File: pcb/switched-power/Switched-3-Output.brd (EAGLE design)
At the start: 100 x 80 mm, 39 parts, among them SW1 SPDT-100SP4, SW2 SPDT-100SP4, SW3 SPDT-100SP4

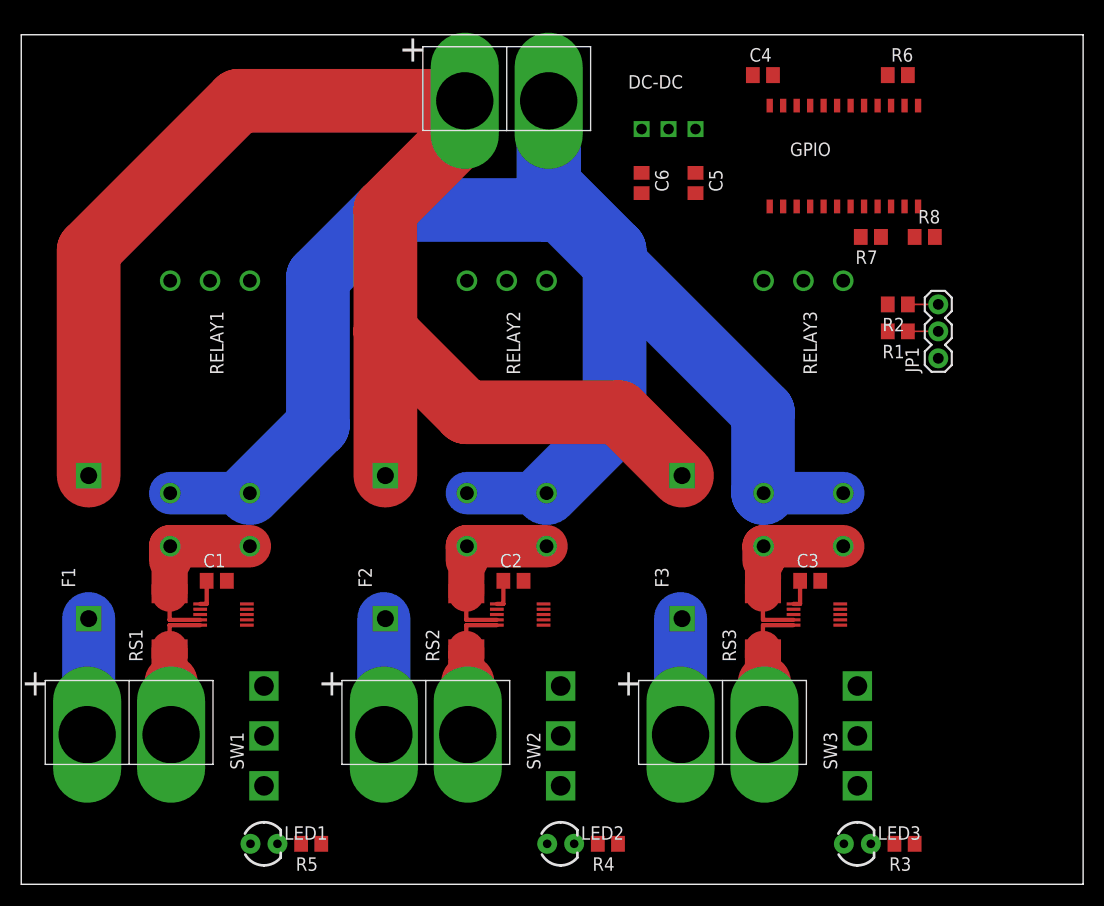
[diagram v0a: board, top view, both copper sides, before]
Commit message: Add gitignore, plus make new revision with latest board
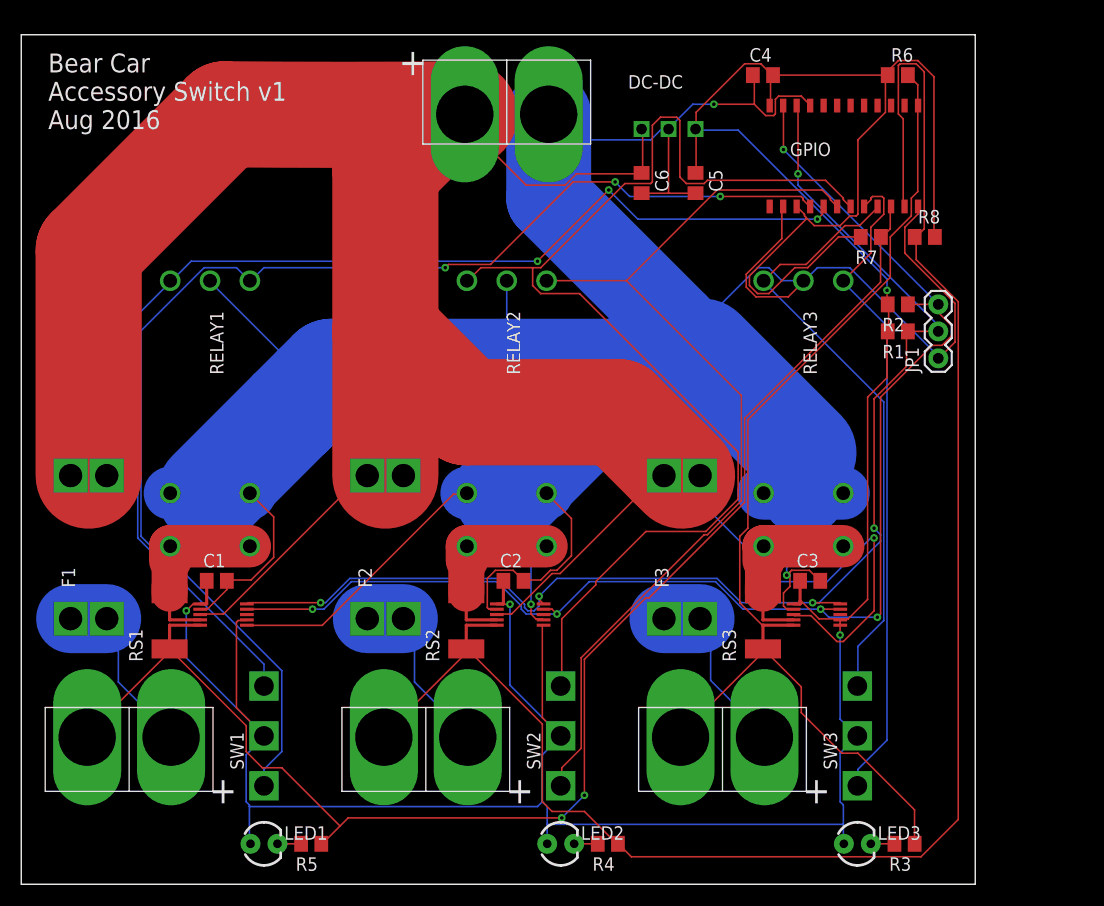
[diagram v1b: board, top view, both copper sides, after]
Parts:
- R1, R2: value (none) -> 2k
- R3, R4, R5: value (none) -> 97.6
- R6, R7, R8: value (none) -> 5k
- moved VSW1 2.54 mm to (10.2, 12.7), turned to 180 degrees
- moved VSW2 2.54 mm to (38.1, 12.7), turned to 180 degrees
- moved VSW3 2.54 mm to (66.0, 12.7), turned to 180 degrees
- moved PWR 1.27 mm to (45.7, 73.7)
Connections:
- removed net N$15: GPIO.1
- net V24: now also F1.B@1, F1.B@2, F2.B@1, F2.B@2, F3.B@1, F3.B@2; no longer F1.P$2, F2.P$2, F3.P$2
- net VSW1+: now also F1.A@1, F1.A@2; no longer F1.P$1
- net VSW2+: now also F2.A@1, F2.A@2; no longer F2.P$1
- net VSW3+: now also F3.A@1, F3.A@2; no longer F3.P$1
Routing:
- net V5: track 8.37 -> 320.8 mm, vias 0 -> 4
- net GND: track 167.5 -> 366.2 mm, vias 0 -> 3
- net VSW2-: track 14.0 -> 166.5 mm
- net SDA: track 2.86 -> 128.9 mm, vias 0 -> 5
- net VSW1-: track 14.0 -> 136.1 mm, vias 0 -> 2
- net V24: track 134.4 -> 255.2 mm, vias 0 -> 1
- net RLY1-ON: track 0.00 -> 120.3 mm, vias 0 -> 3
- net SCL: track 2.86 -> 121.9 mm, vias 0 -> 5
- net RLY2-OFF: track 0.00 -> 112.4 mm
- net RLY1-OFF: track 0.00 -> 111.4 mm, vias 0 -> 3
- net RLY2-ON: track 0.00 -> 91.0 mm
- net VSW3-: track 14.0 -> 102.6 mm
- net RLY3-ON: track 0.00 -> 62.2 mm
- net RLY3-OFF: track 0.00 -> 57.5 mm
- net VSW2+: track 11.1 -> 18.4 mm
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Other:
- board size 100 x 80 mm -> 89.8 x 80 mm
- board text added: "Bear Car Accessory Switch v1 Aug 2016"
- board text added: "Switched 1"
- board text added: "Switched 2"
- board text added: "Switched 3"
